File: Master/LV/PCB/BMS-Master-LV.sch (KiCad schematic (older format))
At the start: 26 parts, among them J1 Contactor-, J10 Charge, J11 CAN, J12 USB, J18 OLED, J19 Master, J2 Contactor-, J6 Power Button, J7 Cooling, J8 Discharge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

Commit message: LVupdates
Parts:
- removed J1, J2: Contactor-, ENNOID:EVC500, symbol Device:CircuitBreaker_1P
- removed J9: Precharge, Connectors_Molex:Molex_KK-6410-02_02x2.54mm_Straight, symbol BMS-Master-LV-rescue:Conn_01x02-Connector_Generic-BMS-Master-rescue-BMS-Master-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
- removed R12, R18: 10k, Resistors_SMD:R_2512, symbol Device:R
- added J4: Power, Connector_Phoenix_GMSTB:PhoenixContact_GMSTBVA_2,5_2-G_1x02_P7.50mm_Vertical, symbol BMS-Master-LV-rescue:Conn_01x02-Connector_Generic-BMS-Master-rescue-BMS-Master-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
- added J5: 12V, ENNOID:Pin_1x02-XL, symbol BMS-Master-LV-rescue:Conn_01x02-Connector_Generic-BMS-Master-rescue-BMS-Master-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
- added K1: HE3621A1200, ENNOID:HE3621A1200, symbol ENNOID:HE3621A1200
- BZ1: MPN (none) -> AI-1027-TWT-5V-2-R
- D1, D2: footprint LEDs:LED_0603_HandSoldering -> LED_SMD:LED_0603_1608Metric; MPN (none) -> SML-D12P8WT86C
- J10, J7, J8: footprint Connectors_Molex:Molex_KK-6410-02_02x2.54mm_Straight -> ENNOID:Pin_1x02-XL; MPN (none) -> 70543-0001
- J11, J18, J6: MPN (none) -> 70543-0004
- J12: MPN (none) -> 47346-0001
- J13: renamed from J19; footprint Connectors_Molex:Molex_KK-6410-02_02x2.54mm_Straight -> ENNOID:Pin_1x02-XL; MPN (none) -> 70543-0001
- LOGO1: MPN (none) -> N/A
- Q1: MPN (none) -> BSS138
- R1, R2, R3: footprint Resistors_SMD:R_0603_HandSoldering -> Resistor_SMD:R_0603_1608Metric; MPN (none) -> RC0603JR-07470RL
- R11: footprint Resistors_SMD:R_2512 -> Resistor_SMD:R_2512_6332Metric; MPN (none) -> RC0603FR-0710KL
- R4: footprint Resistors_SMD:R_0603_HandSoldering -> Resistor_SMD:R_0603_1608Metric; MPN (none) -> RC0603JR-071K5L
- R42, R46, R50: footprint Resistors_SMD:R_0603_HandSoldering -> Resistor_SMD:R_0603_1608Metric; MPN (none) -> RC0603JR-074K7L
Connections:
- net +12V: now also J5.1 (Pin_1), K1.3
- net GND: now also J4.2 (Pin_2), J5.2 (Pin_2)
- net MCU/OLED_RST: now also J18.3 (Pin_3); no longer J18.2 (Pin_2)
- net MCU/OLED_SDA: now also J18.2 (Pin_2); no longer J18.3 (Pin_3)
- net PowerMonitor/BAT+: now also J4.1 (Pin_1), K1.4
- net switches/Precharge: now also K1.2
- net at R11.2: now also K1.1
- net PowerMonitor/Load: now reaches R11.1
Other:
- moved on the sheet: R11, R42, R46

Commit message: maintenance update
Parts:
- R11: MPN RC0603FR-0710KL -> 25121WJ0103T4E
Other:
- moved on the sheet: K1, R11
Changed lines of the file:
@@
 Precharge
 Wire Notes Line
-	4625 1350 4625 750
+	4075 1350 4075 150
 Wire Notes Line
-	4625 750  5825 750
+	4050 150  5825 150
 Wire Notes Line
-	5825 750  5825 1350
+	5825 150  5825 1350
 $Comp
 L power:+12V #PWR0112
@@
 ISOLATED
 Wire Notes Line
-	4625 1350 5825 1350
+	4075 1350 5825 1350
 Wire Wire Line
 	7100 5650 7150 5650
@@
 	-1   0    0    -1
 $EndComp
-Wire Wire Line
-	1300 550  1600 550
 $Sheet
 S 4350 1500 1750 1050
@@
 Connection ~ 3700 1000
 Wire Wire Line
-	3700 1000 3775 1000
-Wire Wire Line
 	2875 3600 2925 3600
 Wire Wire Line
@@
 Wire Wire Line
 	2925 3600 4125 3600
-Wire Wire Line
-	2925 600  3775 600
-$Comp
-L ENNOID:HE3621A1200 K1
-U 1 1 5DC5FBE0
-P 4075 800
-F 0 "K1" V 3508 800 50  0000 C CNN
-F 1 "HE3621A1200" V 3599 800 50  0000 C CNN
-F 2 "ENNOID:HE3621A1200" H 4425 750 50  0001 L CNN
-F 3 "" H 4075 800 50  0001 C CNN
-F 4 "HE3621A1200" H 4075 800 50  0001 C CNN "MPN"
-	1    4075 800
-	0    1    1    0
-$EndComp
-Wire Wire Line
-	4375 1000 4625 1000
-Wire Wire Line
-	4375 600  6925 600
 $Comp
 L Device:R R?
 U 1 1 5DC7CD7E
-P 4775 1000
+P 5525 1000
 AR Path="/5C519BA0/5DC7CD7E" Ref="R?"  Part="1"
 AR Path="/5D7DC460/5DC7CD7E" Ref="R?"  Part="1"
 AR Path="/5DC7CD7E" Ref="R11"  Part="1"
-F 0 "R11" V 4568 1000 50  0000 C CNN
-F 1 "10k" V 4659 1000 50  0000 C CNN
-F 2 "Resistor_SMD:R_2512_6332Metric" V 4705 1000 50  0001 C CNN
-F 3 "~" H 4775 1000 50  0001 C CNN
-F 4 "RC0603FR-0710KL" H 4775 1000 50  0001 C CNN "MPN"
-	1    4775 1000
+F 0 "R11" V 5318 1000 50  0000 C CNN
+F 1 "10k" V 5409 1000 50  0000 C CNN
+F 2 "Resistor_SMD:R_2512_6332Metric" V 5455 1000 50  0001 C CNN
+F 3 "~" H 5525 1000 50  0001 C CNN
+F 4 "25121WJ0103T4E" H 5525 1000 50  0001 C CNN "MPN"
+	1    5525 1000
 	0    1    1    0
 $EndComp
 Wire Wire Line
-	4925 1000 6300 1000
+	5675 1000 6300 1000
 $Sheet
 S 7150 3500 1550 6600
@@
 Wire Wire Line
 	4125 3600 4350 3600
+Wire Wire Line
+	3700 1000 4575 1000
+Wire Wire Line
+	5175 1000 5375 1000
+Wire Wire Line
+	5175 600  6925 600
+Wire Wire Line
+	2925 600  4575 600
+$Comp
+L ENNOID:HE3621A1200 K1
+U 1 1 5DC5FBE0
+P 4875 800
+F 0 "K1" V 4308 800 50  0000 C CNN
+F 1 "HE3621A1200" V 4399 800 50  0000 C CNN
+F 2 "ENNOID:HE3621A1200" H 5225 750 50  0001 L CNN
+F 3 "" H 4875 800 50  0001 C CNN
+F 4 "HE3621A1200" H 4875 800 50  0001 C CNN "MPN"
+	1    4875 800
+	0    1    1    0
+$EndComp
 $EndSCHEMATC

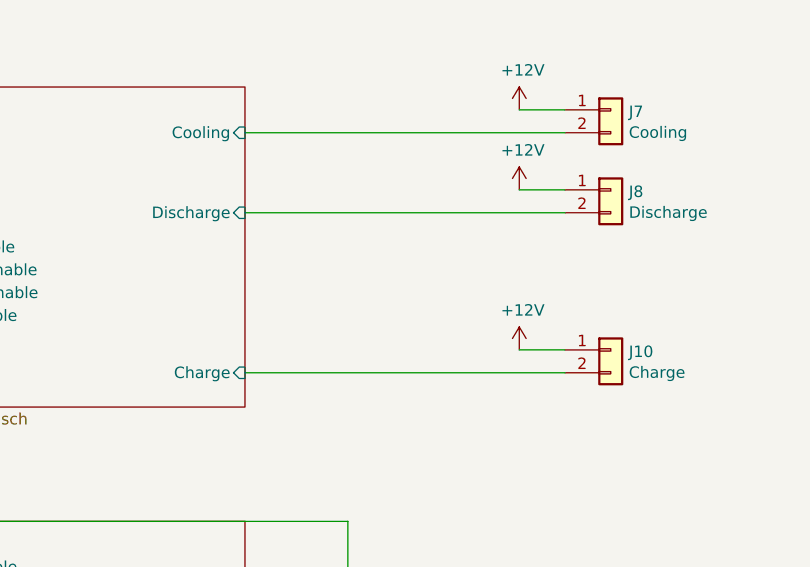
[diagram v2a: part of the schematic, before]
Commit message: Small changes to resistor & connectors
Now with vertical USB connectors & clip connectors
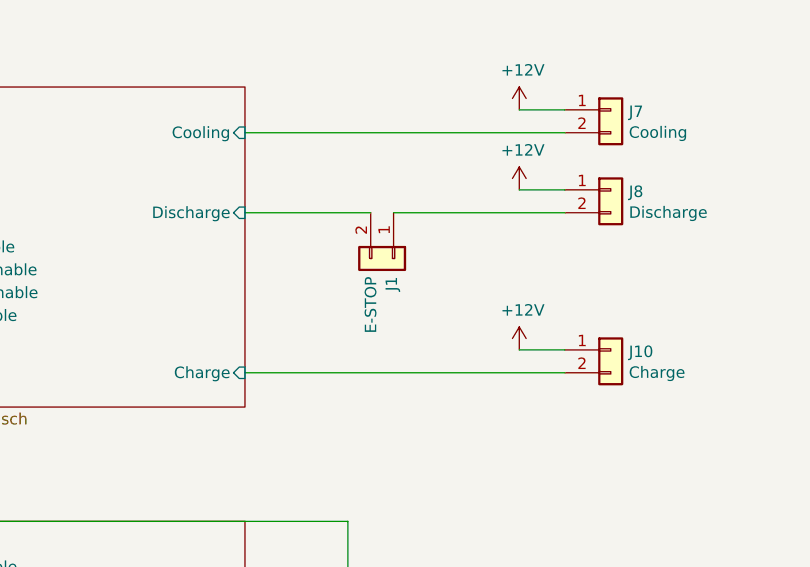
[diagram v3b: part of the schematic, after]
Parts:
- added J1: E-STOP, ENNOID:Pin_1x02-XL, symbol BMS-Master-LV-rescue:Conn_01x02-Connector_Generic-BMS-Master-rescue-BMS-Master-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
- J12: footprint Connectors_USB:USB_Micro-B_Molex_47346-0001 -> Connector_USB:USB_Micro-B_Molex-105133-0001
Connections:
- net switches/Discharge: now also J1.2 (Pin_2); no longer J8.2 (Pin_2)
- new net: J1.1 (Pin_1), J8.2 (Pin_2)
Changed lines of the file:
@@
 F 0 "J12" H 11906 7217 50  0000 C CNN
 F 1 "USB" H 11906 7126 50  0000 C CNN
-F 2 "Connectors_USB:USB_Micro-B_Molex_47346-0001" H 12000 6700 50  0001 C CNN
+F 2 "Connector_USB:USB_Micro-B_Molex-105133-0001" H 12000 6700 50  0001 C CNN
 F 3 "~" H 12000 6700 50  0001 C CNN
 F 4 "47346-0001" H 11850 6750 50  0001 C CNN "MPN"
@@
 	8700 1800 10100 1800
 Wire Wire Line
-	8700 2150 10100 2150
-Wire Wire Line
 	9900 2750 10100 2750
 Wire Wire Line
-	9900 2050 10100 2050
-Wire Wire Line
 	9900 1700 10100 1700
 Wire Wire Line
 	8700 2850 10100 2850
-$Comp
-L power:+12V #PWR0113
-U 1 1 5DC826DE
-P 9900 2050
-F 0 "#PWR0113" H 9900 1900 50  0001 C CNN
-F 1 "+12V" H 9915 2223 50  0000 C CNN
-F 2 "" H 9900 2050 50  0001 C CNN
-F 3 "" H 9900 2050 50  0001 C CNN
-	1    9900 2050
-	1    0    0    -1
-$EndComp
 $Comp
 L power:+12V #PWR0115
@@
 	0    1    1    0
 $EndComp
+Wire Wire Line
+	9350 2150 10100 2150
+Wire Wire Line
+	8700 2150 9250 2150
+Wire Wire Line
+	9900 2050 10100 2050
+$Comp
+L BMS-Master-LV-rescue:Conn_01x02-Connector_Generic-BMS-Master-rescue-BMS-Master-rescue J1
+U 1 1 5E2A5206
+P 9350 2350
+F 0 "J1" H 9429 2342 50  0000 L CNN
+F 1 "E-STOP" H 9429 2251 50  0000 L CNN
+F 2 "ENNOID:Pin_1x02-XL" H 9350 2350 50  0001 C CNN
+F 3 "~" H 9350 2350 50  0001 C CNN
+F 4 "70543-0001 " H 9350 2350 50  0001 C CNN "MPN"
+	1    9350 2350
+	0    1    1    0
+$EndComp
+$Comp
+L power:+12V #PWR0113
+U 1 1 5DC826DE
+P 9900 2050
+F 0 "#PWR0113" H 9900 1900 50  0001 C CNN
+F 1 "+12V" H 9915 2223 50  0000 C CNN
+F 2 "" H 9900 2050 50  0001 C CNN
+F 3 "" H 9900 2050 50  0001 C CNN
+	1    9900 2050
+	1    0    0    -1
+$EndComp
 $EndSCHEMATC

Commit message: Minor changes to charging detect circuit for external relay
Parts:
- J4: footprint Connector_Phoenix_GMSTB:PhoenixContact_GMSTBVA_2,5_2-G_1x02_P7.50mm_Vertical -> Connector_Phoenix_MC_HighVoltage:PhoenixContact_MCV_1,5_2-G-5.08_1x02_P5.08mm_Vertical
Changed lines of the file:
@@
 F 0 "J4" H 3404 992 50  0000 L CNN
 F 1 "Power" H 3404 901 50  0000 L CNN
-F 2 "Connector_Phoenix_GMSTB:PhoenixContact_GMSTBVA_2,5_2-G_1x02_P7.50mm_Vertical" H 3325 1000 50  0001 C CNN
+F 2 "Connector_Phoenix_MC_HighVoltage:PhoenixContact_MCV_1,5_2-G-5.08_1x02_P5.08mm_Vertical" H 3325 1000 50  0001 C CNN
 F 3 "~" H 3325 1000 50  0001 C CNN
 F 4 "30.102 " H 3325 1000 50  0001 C CNN "MPN"

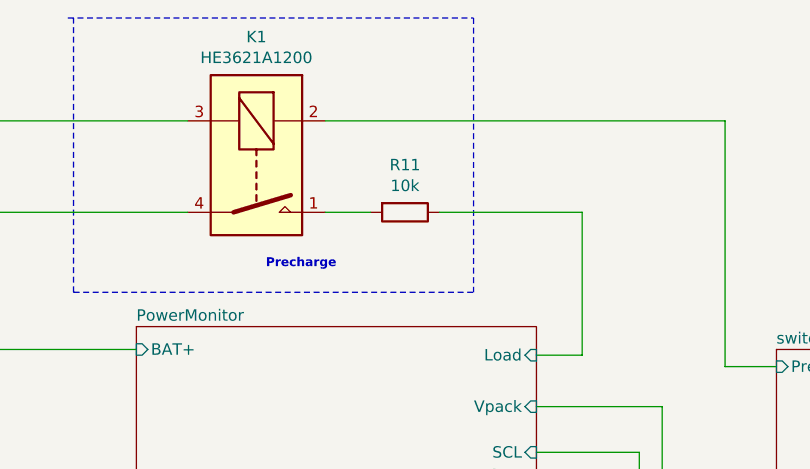
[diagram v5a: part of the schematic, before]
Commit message: New parts for precharge circuit
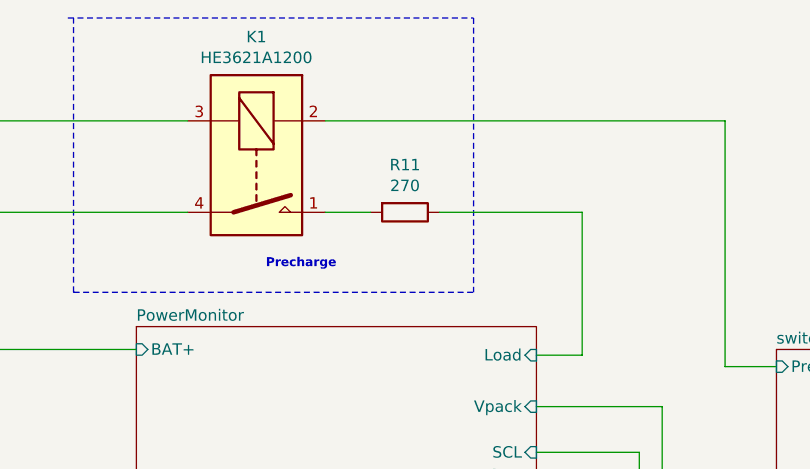
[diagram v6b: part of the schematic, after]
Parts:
- R11: value 10k -> 270; footprint Resistor_SMD:R_2512_6332Metric -> ENNOID:SM_3; MPN 25121WJ0103T4E -> SMW3270RJT
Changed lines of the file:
@@
 AR Path="/5DC7CD7E" Ref="R11"  Part="1"
 F 0 "R11" V 5318 1000 50  0000 C CNN
-F 1 "10k" V 5409 1000 50  0000 C CNN
-F 2 "Resistor_SMD:R_2512_6332Metric" V 5455 1000 50  0001 C CNN
+F 1 "270" V 5409 1000 50  0000 C CNN
+F 2 "ENNOID:SM_3" V 5455 1000 50  0001 C CNN
 F 3 "~" H 5525 1000 50  0001 C CNN
-F 4 "25121WJ0103T4E" H 5525 1000 50  0001 C CNN "MPN"
+F 4 "SMW3270RJT" H 5525 1000 50  0001 C CNN "MPN"
 	1    5525 1000
 	0    1    1    0

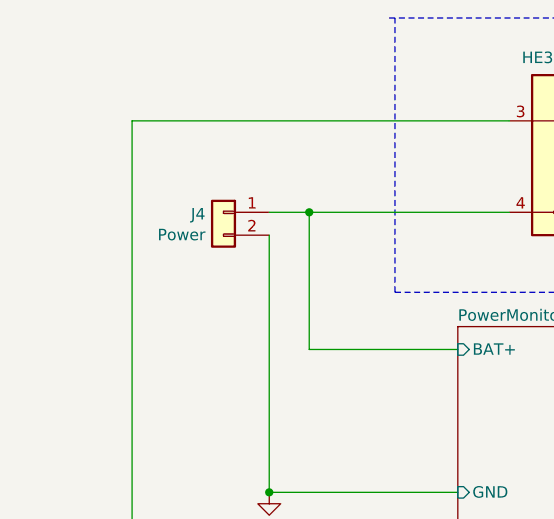
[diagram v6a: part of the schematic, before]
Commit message: Transient voltage suppressor changes
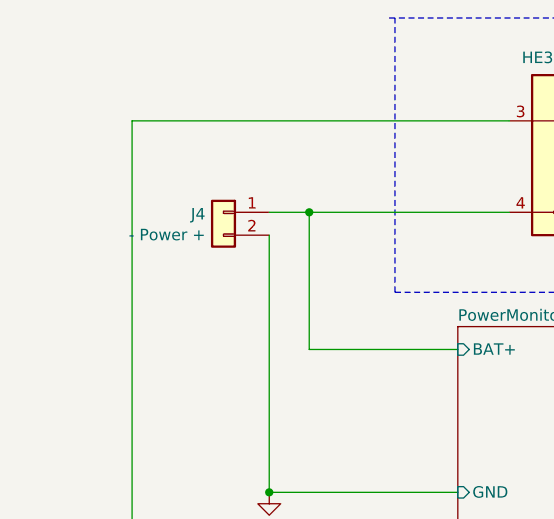
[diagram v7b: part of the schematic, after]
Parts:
- J4: value Power -> - Power +
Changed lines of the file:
@@
 P 3325 1000
 F 0 "J4" H 3404 992 50  0000 L CNN
-F 1 "Power" H 3404 901 50  0000 L CNN
+F 1 "- Power +" H 3404 901 50  0000 L CNN
 F 2 "Connector_Phoenix_MC_HighVoltage:PhoenixContact_MCV_1,5_2-G-5.08_1x02_P5.08mm_Vertical" H 3325 1000 50  0001 C CNN
 F 3 "~" H 3325 1000 50  0001 C CNN
